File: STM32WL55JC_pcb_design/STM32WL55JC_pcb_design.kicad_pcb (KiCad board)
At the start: 2 copper layers, 125 parts, among them IC1 STM32F051R8T6, IC2 CY8C9540A-24PVXIT, IC3 SX1276IMLTRT, IC4 PE4259, IC5 PE4259, IC6 HTS221TR, J1 Conn_01x03, J10 Conn_01x08_Male, J11 Conn_02x02_Odd_Even, J12 Conn_01x10, J13 Conn_01x10, J14 Conn_01x10, J15 Conn_01x10, J16 Conn_Coaxial, J17 Conn_Coaxial, J18 CT3151-2, J19 CT3151-2, J2 Conn_01x03, J20 USB-A-S-F-B-TH, J21 Conn_02x02_Odd_Even, J22 Conn_01x20_Male, J3 Conn_01x03, J4 Conn_01x09, J5 Conn_01x09, J6 Conn_01x03, J7 Conn_01x09, J8 Conn_01x09, J9 Conn_02x10_Odd_Even, Q1 AO3401A, SW1 SW_MEC_5E, SW2 SW_MEC_5E, U2 L80-M39, U3 LIS3DHTR, U4 AMS1117-3.3, U5 AMS1117-5.0, Y1 32MHz, Y2 32.768kHz, Y3 32MHz

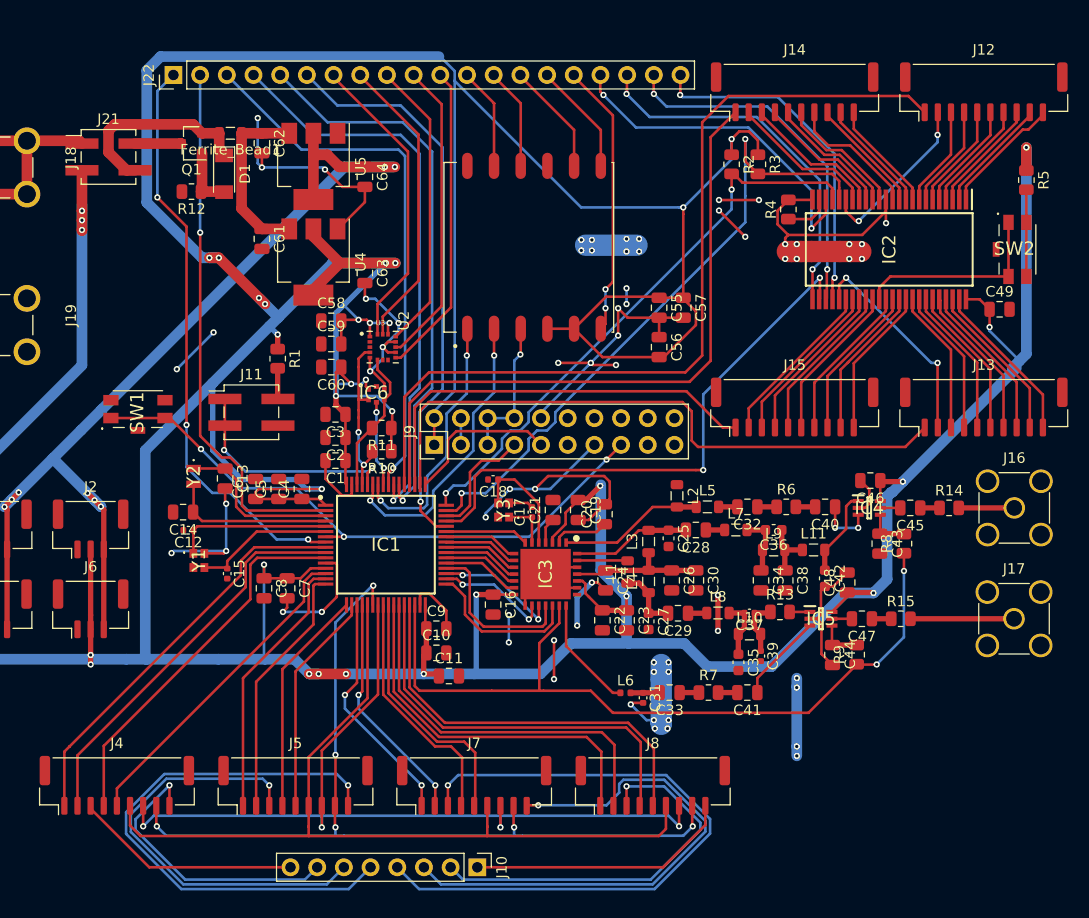
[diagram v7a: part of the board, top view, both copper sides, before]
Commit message: Change devices to available ones from JLC
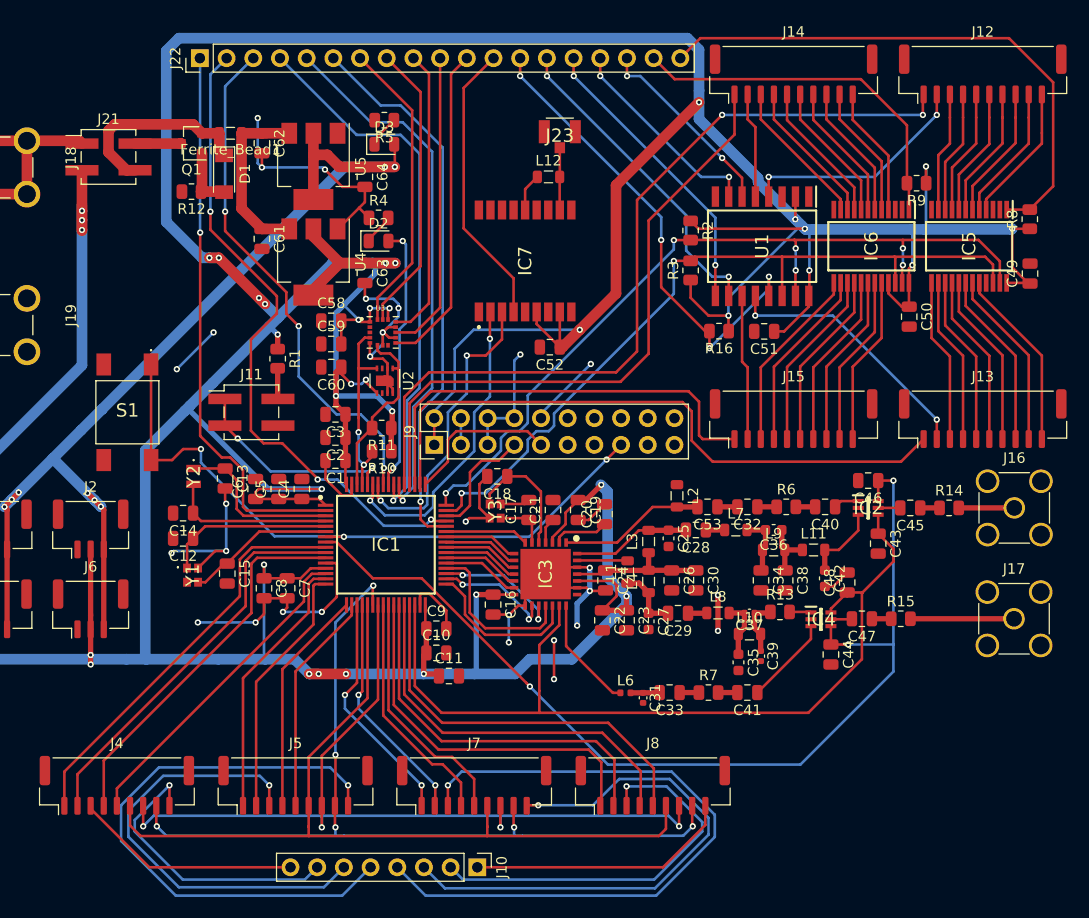
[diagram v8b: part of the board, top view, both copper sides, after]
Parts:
- removed C55, C56: 100nF, Capacitor_SMD:C_0805_2012Metric
- removed C57: 10uF, Capacitor_SMD:C_0805_2012Metric
- removed L5: 4.7pH, Inductor_SMD:L_0805_2012Metric
- removed SW1, SW2: SW_MEC_5E, EVQ-P2F02K:EVQP2V02W
- added C50: 100nF, Capacitor_SMD:C_0805_2012Metric, F.Cu at (189.3, 64.2)
- added C51: 100nF, Capacitor_SMD:C_0805_2012Metric, F.Cu at (175.5, 65.6)
- added C52: 10uF, Capacitor_SMD:C_0805_2012Metric, F.Cu at (155.1, 67.1)
- added C53: 4.7pF, Capacitor_SMD:C_0805_2012Metric, F.Cu at (170.1, 82.3)
- added D2: LED, LED_SMD:LED_0805_2012Metric, F.Cu at (138.8, 57.0)
- added D3: LED, LED_SMD:LED_0805_2012Metric, F.Cu at (139.3, 47.8)
- added IC7: ATGM336H-5N31, ATGM336H-5N31:ATGM336H5N31, F.Cu at (152.8, 58.9)
- added J23: RSP-122811-01, HC-RF-IPEX0303:RSP12281101, F.Cu at (156.1, 46.6)
- added L12: 47nH, Inductor_SMD:L_0805_2012Metric, F.Cu at (155.0, 50.9)
- added R16: 2.2k, Resistor_SMD:R_0805_2012Metric, F.Cu at (171.2, 65.6)
- added S1: TL3301AF160QJ, TL3301AF160QJ:TL3301AF160QJ, F.Cu at (114.9, 73.3)
- added U1: PCF8574, PCF8574T_3_518:SOIC127P1032X265-16N, F.Cu at (175.3, 57.5)
- C12, C15, C17, C18: value 13pF -> 10pF; footprint Capacitor_SMD:C_0402_1005Metric -> Capacitor_SMD:C_0805_2012Metric
- IC2: value CY8C9540A-24PVXIT -> CG2409M2; footprint CY8C9540A-24PVXIT:SOP64P1035X279-48N -> CKRF2406XS03-C2:CKRF2406XS03-C2
- IC4: value PE4259 -> CG2409M2; footprint PE4259:SOT65P210X110-6N -> CKRF2406XS03-C2:CKRF2406XS03-C2
- IC5: value PE4259 -> PCF8575TS_1,118; footprint PE4259:SOT65P210X110-6N -> PCF8575TS_1_118:SOP65P775X200-24N
- IC6: value HTS221TR -> PCF8575TS_1,118; footprint HTS221TR:HTS221TR -> PCF8575TS_1_118:SOP65P775X200-24N
- J22: value Conn_01x20_Male -> Conn_01x19_Male; footprint Connector_PinHeader_2.54mm:PinHeader_1x20_P2.54mm_Vertical -> Connector_PinHeader_2.54mm:PinHeader_1x19_P2.54mm_Vertical
- R4: value 200 -> 1k
- R8, R9: value 1k -> 2.2k
- U2: value L80-M39 -> SHT30-DIS; footprint L80-M39:XCVR_L80-M39 -> Sensor_Humidity:Sensirion_DFN-8-1EP_2.5x2.5mm_P0.5mm_EP1.1x1.7mm
- moved R5 61.4 mm to (139.3, 45.5), turned to 180 degrees
- moved IC6 49.2 mm to (185.7, 57.5), turned to 270 degrees
- moved R9 45.2 mm to (190.0, 51.5), turned to 180 degrees
- moved R4 39.0 mm to (138.8, 54.8), turned to 0 degrees
- moved IC5 38.2 mm to (195.0, 57.5), turned to 270 degrees
- moved R8 33.1 mm to (200.8, 54.9)
- moved IC2 24.7 mm to (185.4, 82.4), turned to 0 degrees
- moved U2 19.1 mm to (139.4, 70.3), turned to 270 degrees
- moved R3 12.0 mm to (168.5, 59.8), turned to 90 degrees
- moved IC4 11.6 mm to (180.9, 93.0)
- moved R2 7.41 mm to (168.5, 56.0)
- moved C49 4.47 mm to (200.8, 60.1), turned to 90 degrees
- moved J22 2.99 mm to (121.8, 39.6)
- moved J12 1.70 mm to (196.3, 41.1)
- moved J14 1.70 mm to (178.3, 41.1)
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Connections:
- C43 pad 1: Net-(C43-Pad1) -> LoRa_TX_EN
- C44 pad 1: Net-(C44-Pad1) -> LoRa_RX_EN
- C46 pad 1: VDD -> LoRa_RX_EN
- C48 pad 1: VDD -> LoRa_TX_EN
- IC1 pad 30: LoRa_RXTX_CTRL -> LoRa_TX_EN
- IC1 pad 45: EXP_INT -> PA12
- IC1 pad 56: PB4 -> Net-(D2-Pad2)
- IC1 pad 57: TempHumid_DRDY -> PB5
- IC1 pad 8: PC0 -> LoRa_RX_EN
- IC2 pad 1: ENC1_1 -> Net-(C40-Pad1)
- IC2 pad 2: ENC1_2 -> GNDREF
- IC2 pad 3: ENC1_3 -> Net-(C42-Pad1)
- IC2 pad 4: ENC1_4 -> LoRa_TX_EN
- IC2 pad 5: ENC2_1 -> Net-(C45-Pad2)
- IC2 pad 6: ENC2_2 -> LoRa_RX_EN
- IC3 pad 20: LoRa_RXTX_CTRL -> LoRa_TX_EN
- IC4 pad 1: Net-(C42-Pad1) -> Net-(IC4-Pad1)
- IC4 pad 3: Net-(C40-Pad1) -> Net-(C41-Pad1)
- IC4 pad 4: Net-(C43-Pad1) -> LoRa_RX_EN
- IC4 pad 5: Net-(C45-Pad2) -> Net-(C47-Pad2)
- IC4 pad 6: VDD -> LoRa_TX_EN
- IC5 pad 1: Net-(IC5-Pad1) -> EXP_INT1
- IC5 pad 3: Net-(C41-Pad1) -> GNDREF
- IC5 pad 4: Net-(C44-Pad1) -> ENC1_1
- IC5 pad 5: Net-(C47-Pad2) -> ENC1_2
- IC5 pad 6: VDD -> ENC1_3
- IC6 pad 1: VDD -> EXP_INT2
- IC6 pad 2: SCL -> GNDREF
- IC6 pad 3: TempHumid_DRDY -> GNDREF
- IC6 pad 4: SDA -> ENC3_1
- IC6 pad 5: GNDREF -> ENC3_2
- IC6 pad 6: Net-(IC6-Pad6) -> ENC3_3
- J22 pad 1: PC0 -> PC13
- J22 pad 12: GPS_EX_ANT -> GPS_1PPS
- J22 pad 13: GPS_RESET -> EXP_INT3
- J22 pad 14: GPS_AADET_N -> EXP_P5
- J22 pad 15: GPS_TIMER -> EXP_P4
- J22 pad 16: GPS_1PPS -> EXP_P3
- J22 pad 17: EXP_3 -> EXP_P2
- J22 pad 18: EXP_2 -> EXP_INT2
- J22 pad 19: EXP_1 -> EXP_INT1
- J22 pad 2: PC13 -> PA12
- J22 pad 3: PB4 -> PB5
- R13 pad 2: Net-(IC5-Pad1) -> Net-(IC4-Pad1)
- R4 pad 1: Net-(IC2-Pad23) -> GNDREF
- R4 pad 2: GNDREF -> Net-(D2-Pad1)
- R5 pad 1: VDD -> Net-(D3-Pad1)
- R5 pad 2: Net-(R5-Pad2) -> GNDREF
- R8 pad 1: LoRa_RXTX_CTRL -> VDD
- R8 pad 2: Net-(C43-Pad1) -> EXP_INT1
- R9 pad 1: LoRa_RXTX_CTRL -> VDD
- R9 pad 2: Net-(C44-Pad1) -> EXP_INT2
- U2 pad 1: RX -> SDA
- U2 pad 2: TX -> GNDREF
- U2 pad 3: GNDREF -> Net-(U2-Pad3)
- U2 pad 4: VDD -> SCL
- U2 pad 6: GPS_1PPS -> Net-(U2-Pad6)
- U2 pad 7: GPS_TIMER -> GNDREF
- U2 pad 8: GPS_AADET_N -> GNDREF
- U2 pad 9: (no net) -> GNDREF
- U3 pad 7: Net-(U3-Pad7) -> GNDREF
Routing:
- net LoRa_RX_EN: track 0.00 -> 95.8 mm, vias 0 -> 3
- net LoRa_TX_EN: track 0.00 -> 84.4 mm
- net GNDREF: track 254.8 -> 172.1 mm, vias 67 -> 28
- net LoRa_RXTX_CTRL: track 75.2 -> 0.00 mm, vias 2 -> 0
- net PA12: track 0.00 -> 62.4 mm, vias 0 -> 3
- net PC0: track 55.3 -> 0.00 mm, vias 3 -> 0
- net EXP_INT1: track 0.00 -> 53.2 mm
- net EXP_INT: track 53.2 -> 0.00 mm, vias 2 -> 0
- net PB4: track 52.1 -> 0.00 mm, vias 1 -> 0
- net PB5: track 0.00 -> 49.3 mm, vias 0 -> 3
- net EXP_INT3: track 0.00 -> 46.3 mm, vias 0 -> 4
- net EXP_2: track 35.2 -> 0.00 mm, vias 2 -> 0
- net EXP_INT2: track 0.00 -> 34.9 mm
- net EXP_1: track 33.8 -> 0.00 mm, vias 2 -> 0
- net EXP_0: track 32.8 -> 0.00 mm, vias 2 -> 0
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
